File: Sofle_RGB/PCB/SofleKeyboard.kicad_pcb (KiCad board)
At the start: 2 copper layers, 143.4 x 111.8 mm, 97 parts, among them J1 LED, J2 4PIN, J3 OLED, J4 key leds, J5 backlight sel, J6 indicator bypass, P1 i2c_pin, P2 i2c_pin, SW1 SW_PUSH-MX_W_LED, SW10 SW_PUSH-MX_W_LED, SW11 SW_PUSH-MX_W_LED, SW12 SW_PUSH-MX_W_LED, SW13 SW_PUSH-MX_W_LED, SW14 SW_PUSH-MX_W_LED, SW15 SW_PUSH-MX_W_LED, SW16 SW_PUSH-MX_W_LED, SW17 SW_PUSH-MX_W_LED, SW18 SW_PUSH-MX_W_LED, SW19 SW_PUSH-MX_W_LED, SW2 SW_PUSH-MX_W_LED, SW20 SW_PUSH-MX_W_LED, SW21 SW_PUSH-MX_W_LED, SW22 SW_PUSH-MX_W_LED, SW23 SW_PUSH-MX_W_LED, SW24 SW_PUSH-MX_W_LED, SW25 Rotary_Encoder_Switch, SW26 SW_PUSH-MX_W_LED, SW27 SW_PUSH-MX_W_LED, SW28 SW_PUSH-MX_W_LED, SW29 SW_PUSH-MX_W_LED, SW3 SW_PUSH-MX_W_LED, SW30 SW_PUSH-MX_W_LED, SW4 SW_PUSH-MX_W_LED, SW5 SW_PUSH-MX_W_LED, SW6 SW_PUSH-MX_W_LED, SW7 SW_PUSH-MX_W_LED, SW8 SW_PUSH-MX_W_LED, SW9 SW_PUSH-MX_W_LED, U1 ProMicro

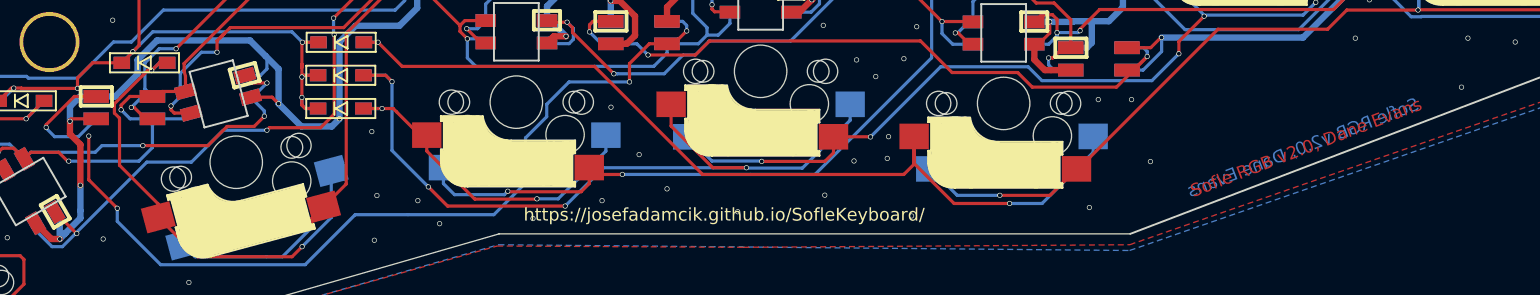
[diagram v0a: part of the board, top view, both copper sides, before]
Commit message: fixed bug in v2.0, upversioned
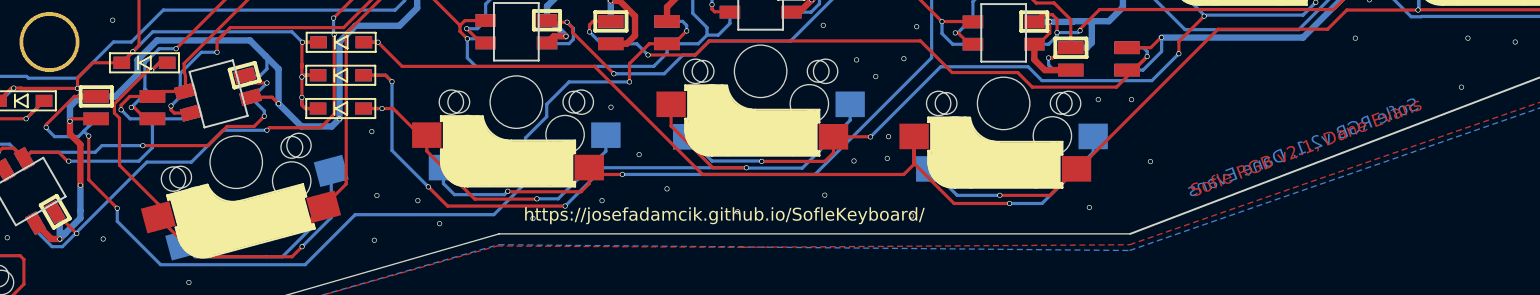
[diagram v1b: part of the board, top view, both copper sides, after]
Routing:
- net Net-(D34-Pad1): track 76.5 -> 77.9 mm
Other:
- board text added: "Sofle RGB v2.1, Dane Evans"
- board text removed: "Sofle RGB v2.0, Dane Evans"
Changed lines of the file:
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@@
     (thickness 1.6)
     (drawings 365)
-    (tracks 3677)
+    (tracks 3681)
     (zones 0)
     (modules 97)
@@
     (34 B.Paste user hide)
     (35 F.Paste user hide)
-    (36 B.SilkS user)
-    (37 F.SilkS user)
-    (38 B.Mask user hide)
+    (36 B.SilkS user hide)
+    (37 F.SilkS user hide)
+    (38 B.Mask user)
     (39 F.Mask user hide)
     (40 Dwgs.User user hide)
@@
     (effects (font (size 1 1) (thickness 0.2)) (justify mirror))
   )
-  (gr_text "Sofle RGB v2.0, Dane Evans" (at 201 127.25 21) (layer B.Cu)
+  (gr_text "Sofle RGB v2.1, Dane Evans" (at 201 127.25 21) (layer B.Cu)
     (effects (font (size 1 1) (thickness 0.2)) (justify mirror))
   )
-  (gr_text "Sofle RGB v2.0, Dane Evans" (at 201.25 127.25 21) (layer F.Cu)
+  (gr_text "Sofle RGB v2.1, Dane Evans" (at 201.25 127.25 21) (layer F.Cu)
     (effects (font (size 1 1) (thickness 0.2)))
   )
@@
   (segment (start 102.74 125.74) (end 102.74 125.6775) (width 0.25) (layer B.Cu) (net 63))
   (segment (start 103.4 126.4) (end 102.74 125.74) (width 0.25) (layer B.Cu) (net 63))
-  (segment (start 106.65 125.005) (end 105.255 126.4) (width 0.25) (layer B.Cu) (net 63))
   (segment (start 105.255 126.4) (end 103.4 126.4) (width 0.25) (layer B.Cu) (net 63))
+  (segment (start 106.06801 125.58699) (end 106.65 125.005) (width 0.25) (layer B.Cu) (net 63))
+  (segment (start 106.65 125.005) (end 105.6675 125.9875) (width 0.25) (layer B.Cu) (net 63))
+  (segment (start 105.704195 125.9875) (end 105.6675 125.9875) (width 0.25) (layer B.Cu) (net 63))
+  (segment (start 105.6675 125.9875) (end 105.255 126.4) (width 0.25) (layer B.Cu) (net 63))
+  (segment (start 106.06801 126.351315) (end 105.704195 125.9875) (width 0.25) (layer B.Cu) (net 63))
   (via (at 188.822468 120.130068) (size 0.4) (drill 0.3) (layers F.Cu B.Cu) (net 64))
   (segment (start 187.25 121.195) (end 187.757536 121.195) (width 0.25) (layer F.Cu) (net 64))

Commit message: Address PR comments + extra cleanup
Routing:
- net GND: track 1001.1 -> 1005.4 mm, vias 230 -> 228
- net VCC: track 928.4 -> 930.1 mm
- net Net-(SW13-Pad1): track 31.7 -> 33.2 mm
- net Net-(SW16-Pad3): track 27.3 -> 28.8 mm
- net Net-(SW19-Pad1): track 4.00 -> 5.17 mm
